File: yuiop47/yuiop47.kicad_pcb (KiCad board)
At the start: 2 copper layers, 214 x 94 mm, 107 parts, among them SW1 SW_PUSH, SW10 SW_PUSH, SW11 SW_PUSH, SW12 SW_PUSH, SW13 SW_PUSH, SW14 SW_PUSH, SW15 SW_PUSH, SW16 SW_PUSH, SW17 SW_PUSH, SW18 SW_PUSH, SW19 SW_PUSH, SW2 SW_PUSH, SW20 SW_PUSH, SW21 SW_PUSH, SW22 SW_PUSH, SW23 SW_PUSH, SW24 SW_PUSH, SW25 SW_PUSH, SW26 SW_PUSH, SW27 SW_PUSH, SW28 SW_PUSH, SW29 SW_PUSH, SW3 SW_PUSH, SW30 SW_PUSH, SW31 SW_PUSH, SW32 SW_PUSH, SW33 SW_PUSH, SW34 SW_PUSH, SW35 SW_PUSH, SW36 SW_PUSH, SW37 SW_PUSH, SW38 SW_PUSH, SW39 SW_PUSH, SW4 SW_PUSH, SW40 SW_PUSH, SW41 SW_PUSH, SW42 SW_PUSH, SW43 SW_PUSH, SW44 SW_PUSH, SW45 SW_PUSH, SW46 SW_PUSH, SW47 SW_PUSH, SW5 SW_PUSH, SW6 SW_PUSH, SW7 SW_PUSH, SW8 SW_PUSH, SW9 SW_PUSH, U1 ProMicro

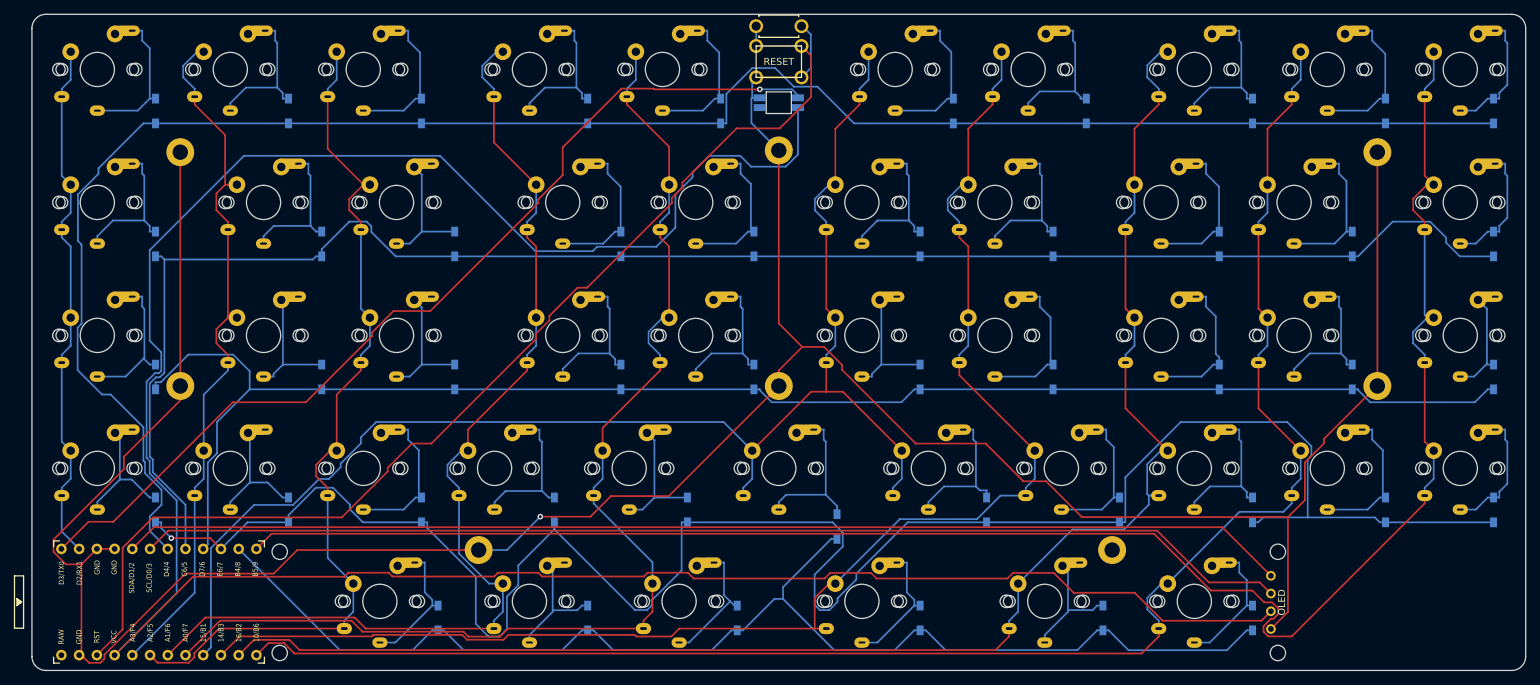
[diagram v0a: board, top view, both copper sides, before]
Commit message: yuiop47: swap LED's VCC/GND
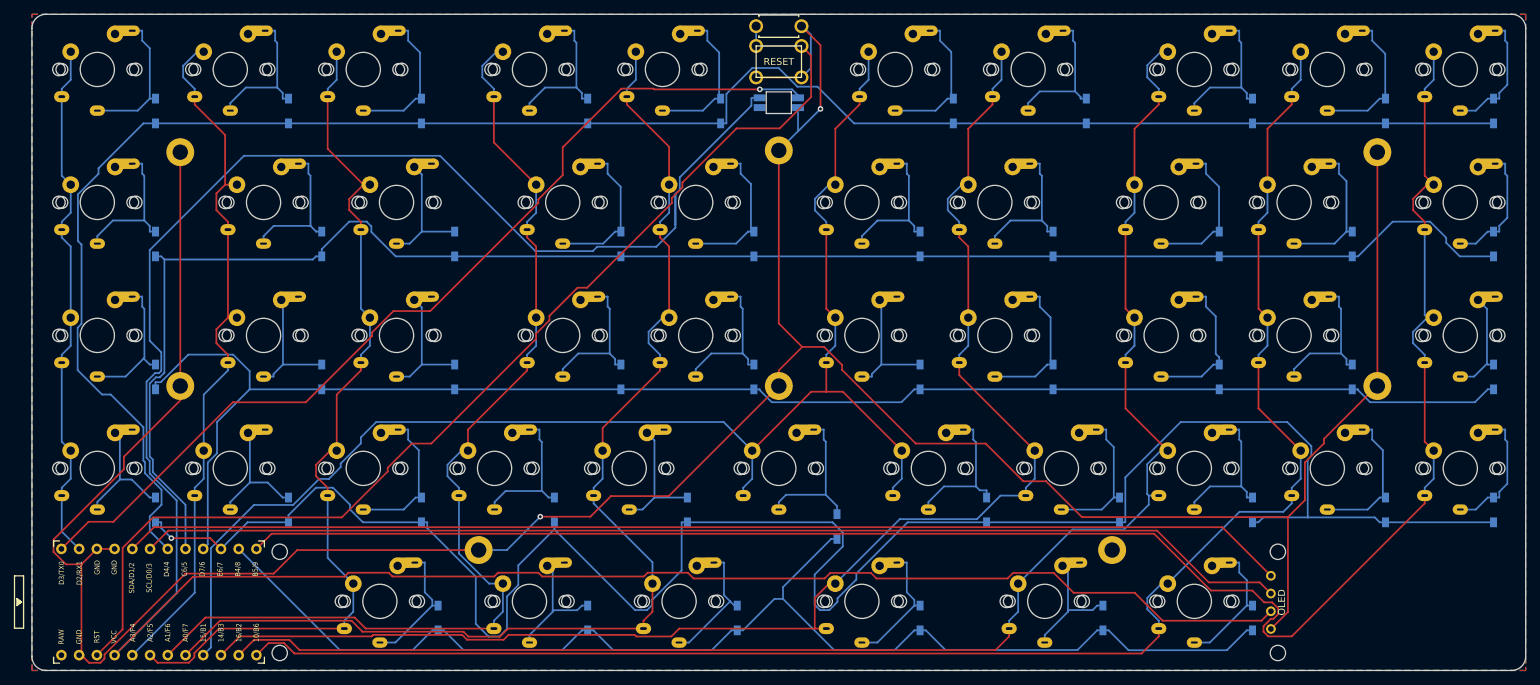
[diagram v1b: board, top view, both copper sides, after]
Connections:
- LED1 pad 1: GND -> VCC
- LED1 pad 3: VCC -> GND
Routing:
- net GND: track 425.5 -> 437.6 mm, vias 1 -> 2
- net VCC: track 362.6 -> 358.1 mm
- added copper zone on B.Cu, net GND
- added copper zone on F.Cu, net GND
